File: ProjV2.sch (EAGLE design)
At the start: 24 parts, among them IC1 CD4007UBM, IC2 CD4007UBM, IC3 CD4007UBM, U1 MIC5504-3.3YM5-T5, U2 MCP2200-I/SS, U3 ATMEGA328PB-AU, U4 EN11-HSM1BF20, Y1 12MHz

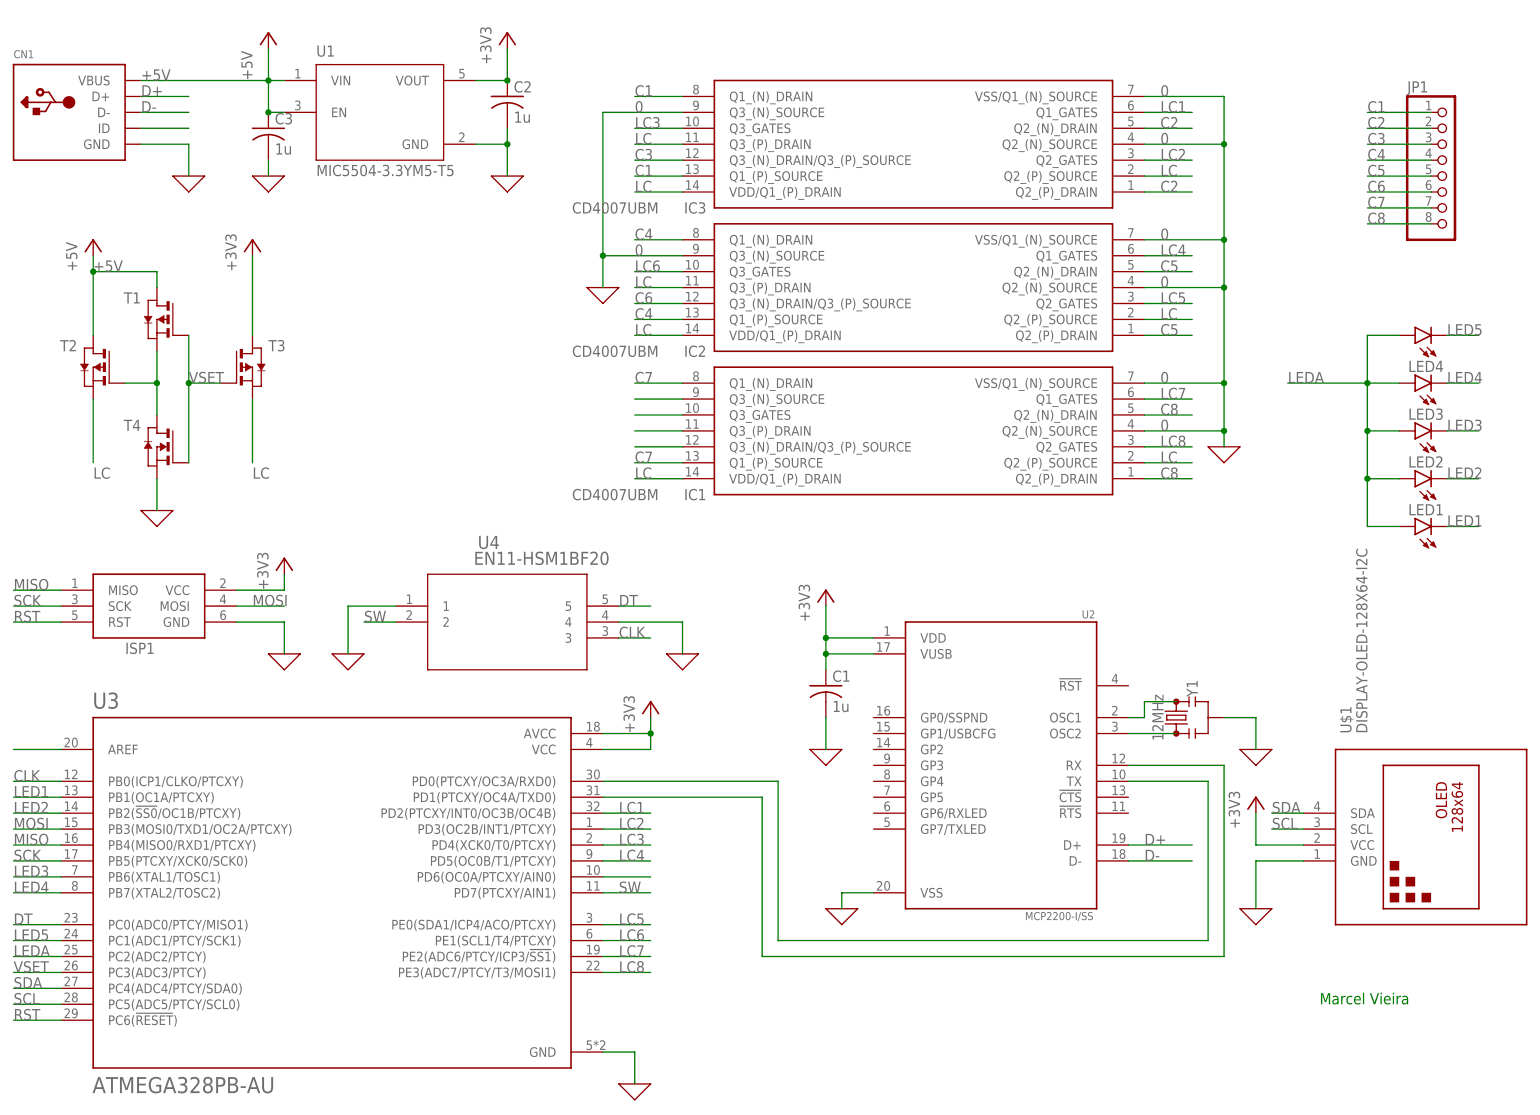
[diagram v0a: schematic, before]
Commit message: Added copies of old versions
Updated version numbers and add old versions for comparison and report writing
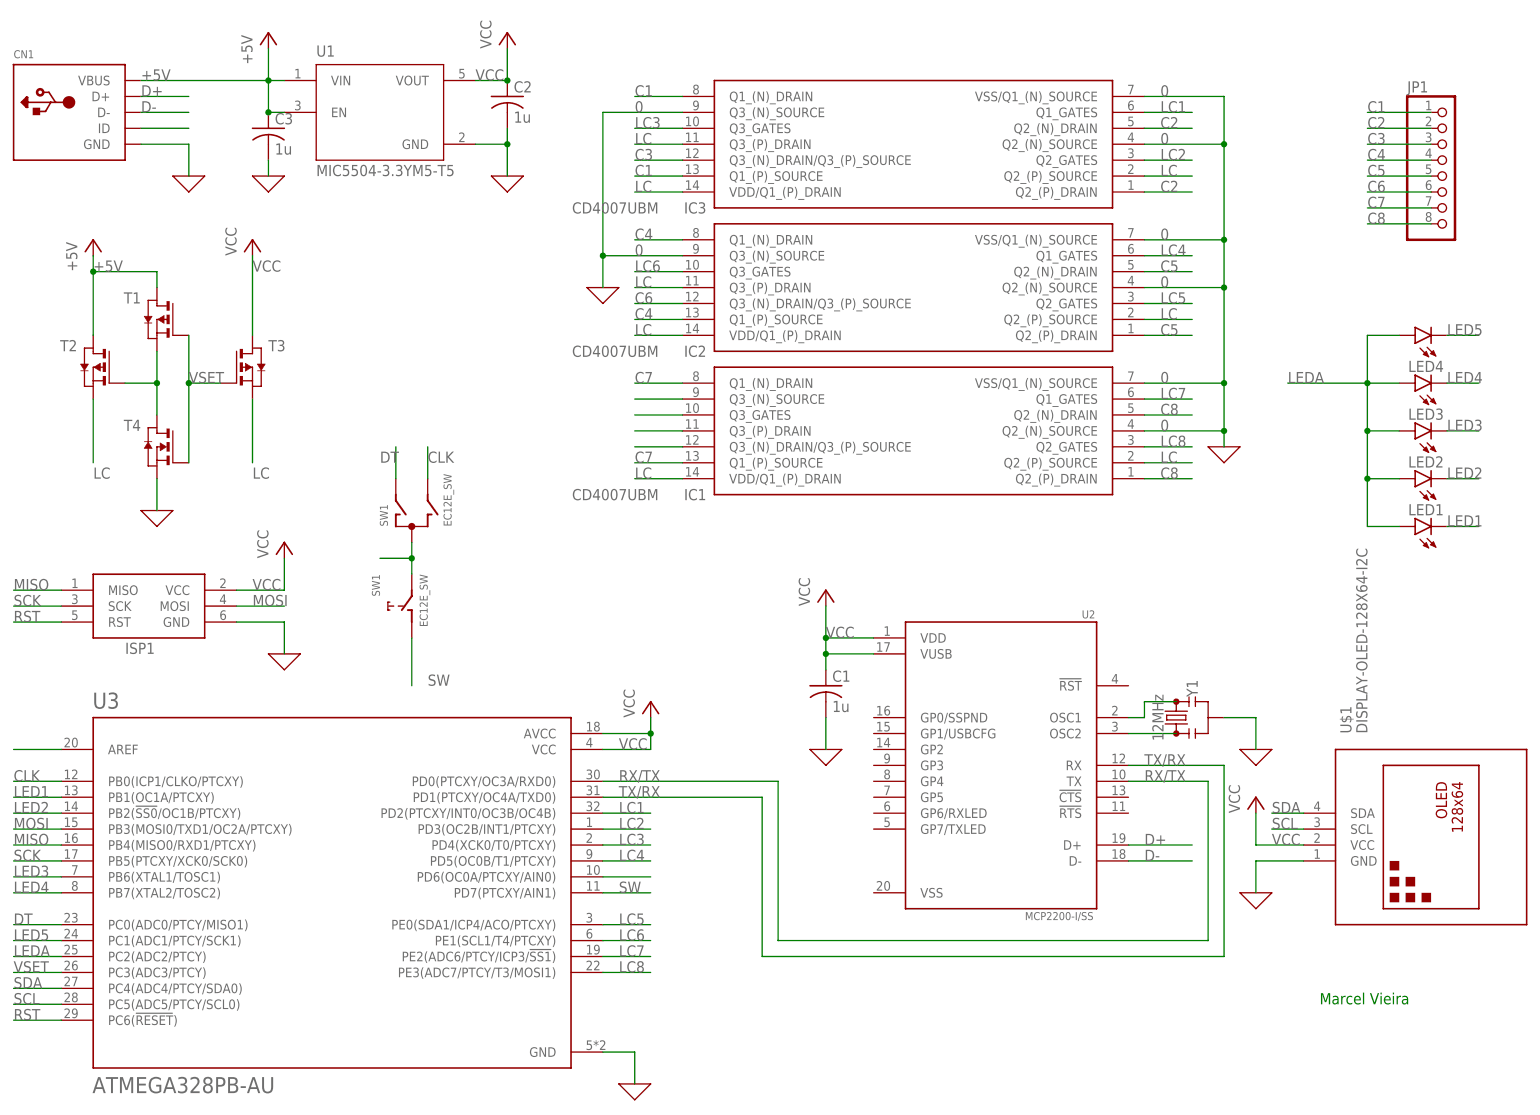
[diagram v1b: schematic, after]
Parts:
- removed U4: EN11-HSM1BF20, EN11-HSM1BF20:EN11-HSM1BF20
- added SW1: EC12E_SW, switch-alps:EC12E_SW
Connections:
- net +3V3 renamed VCC
- new net N$7: SW1G$1.C, SW1G$2.2
- net 0: no longer U2.VSS, U4.1, U4.4
- net CLK: now also SW1G$1.B; no longer U4.3
- net DT: now also SW1G$1.A; no longer U4.5
- net SW: now also SW1G$2.1; no longer U4.2
